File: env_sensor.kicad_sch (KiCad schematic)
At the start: 21 parts, among them J1 E Paper, J3 Barrel_Jack, J4 LED_OUTPUT, J5 Conn_01x02_Pin, J6 Conn_01x04_Socket, J6 ESP_Debugger, Q1 NMOS, Q2 NMOS, Q3 NMOS, U1 ESP32-DevKitC, U1 MH-Z19B, U5 BME280

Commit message: update MOS
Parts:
- Q1, Q2: footprint 2SK4017:TO230P230X650X740-3P -> env-sensor:SOT-23
- Q3: footprint 2SK4017:TO230P230X650X740-3P -> env-sensor:SOT-23; LCSC (none) -> C916396
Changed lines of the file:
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@@
 			)
 		)
-		(property "Footprint" "2SK4017:TO230P230X650X740-3P"
+		(property "Footprint" "env-sensor:SOT-23"
 			(at 58.42 64.77 0)
 			(effects
@@
 			)
 		)
-		(property "Footprint" "2SK4017:TO230P230X650X740-3P"
+		(property "Footprint" "env-sensor:SOT-23"
 			(at 58.42 39.37 0)
 			(effects
@@
 			)
 		)
-		(property "Footprint" "2SK4017:TO230P230X650X740-3P"
+		(property "Footprint" "env-sensor:SOT-23"
 			(at 58.42 90.17 0)
 			(effects
@@
 			)
 		)
-		(property "Sim.Pins" "1=D 2=G 3=S"
+		(property "Sim.Pins" "1=G 2=S 3=D"
 			(at 53.34 107.95 0)
 			(effects
 				(font
+					(size 1.27 1.27)
+				)
+				(hide yes)
+			)
+		)
+		(property "LCSC" "C916396"
+			(at 53.34 92.71 0)
+			(effects
+				(font

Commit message: add drv8847 (Working)
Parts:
- added R4, R5: 330m, Resistor_SMD:R_0603_1608Metric, symbol Device:R
- added U3: DRV8847SPWR, Package_SO:TSSOP-16_4.4x5mm_P0.65mm, symbol Driver_Motor:DRV8847SPWR
- Q1, Q2: LCSC (none) -> C916396
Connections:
- net GND: now also R4.2, R5.2, U3.13 (GND)
- net SCL: now also U3.11 (SCL)
- net SDA: now also U3.14 (SDA)
- new net: R4.1, U3.3 (ISEN12)
- new net: R5.1, U3.6 (ISEN34)

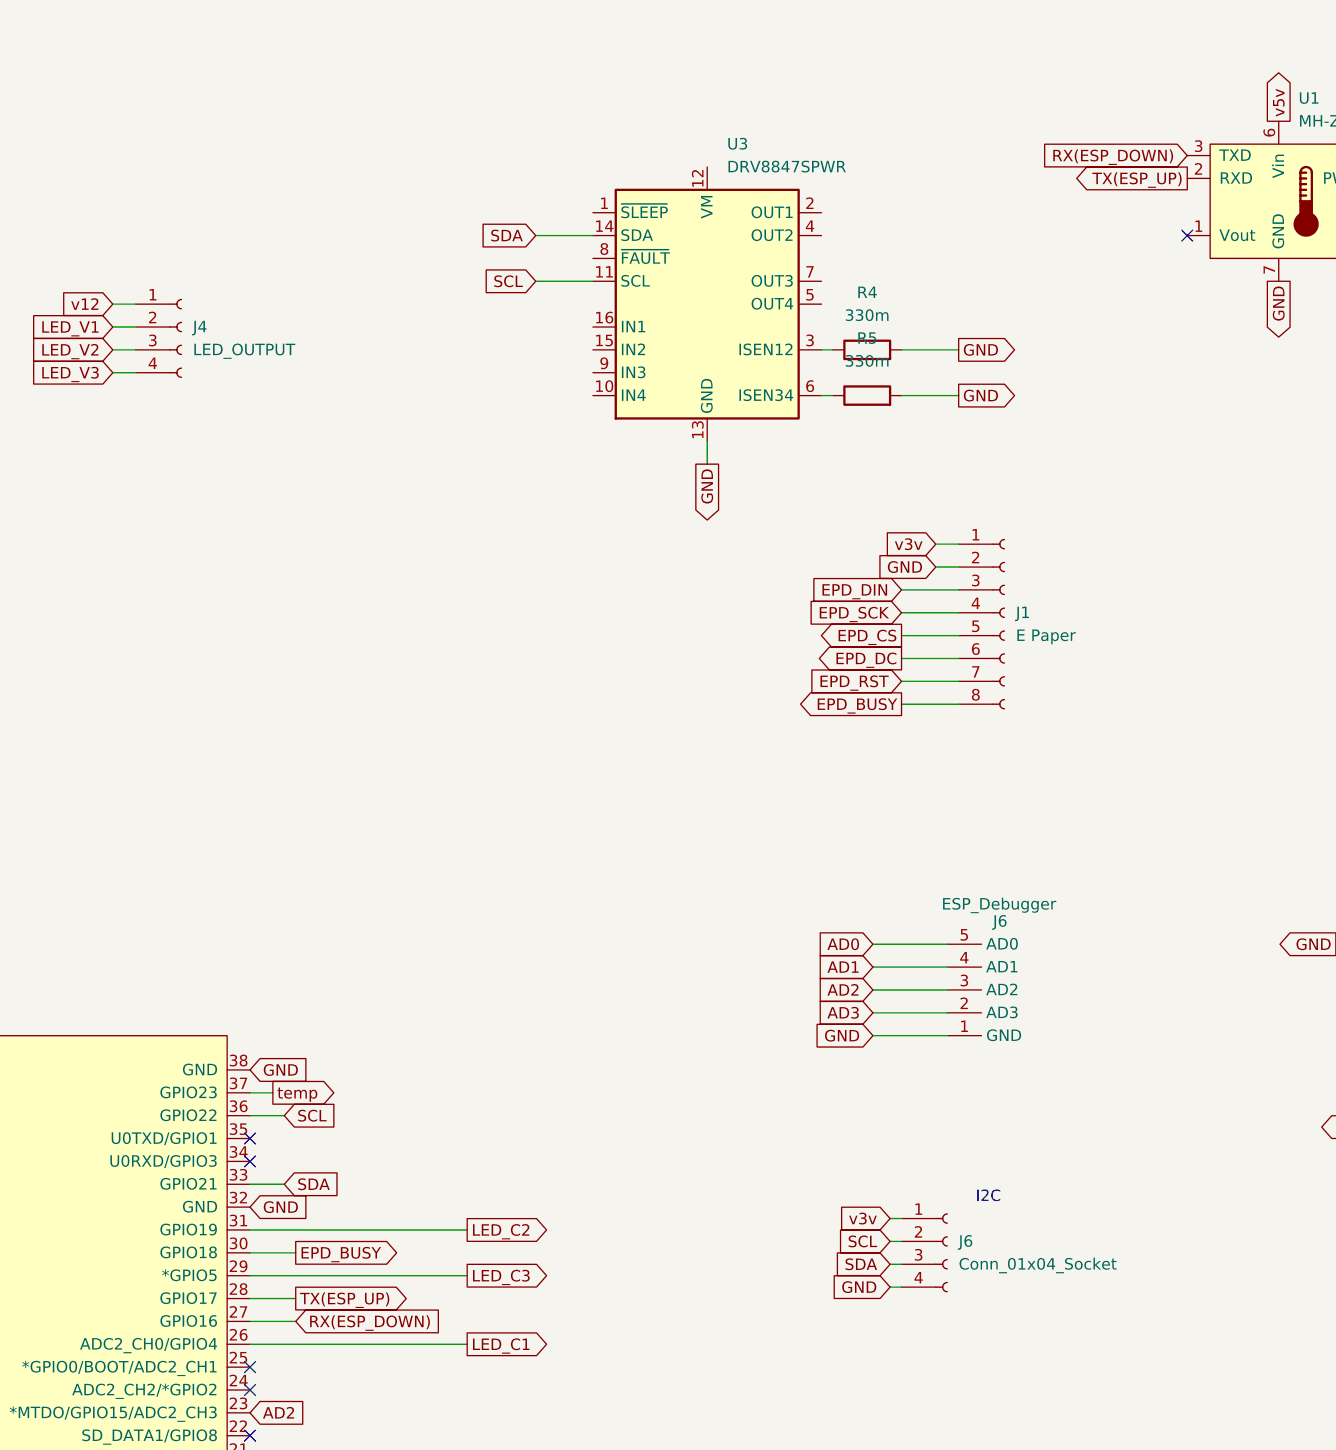
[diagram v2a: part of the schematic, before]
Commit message: add motor drivers
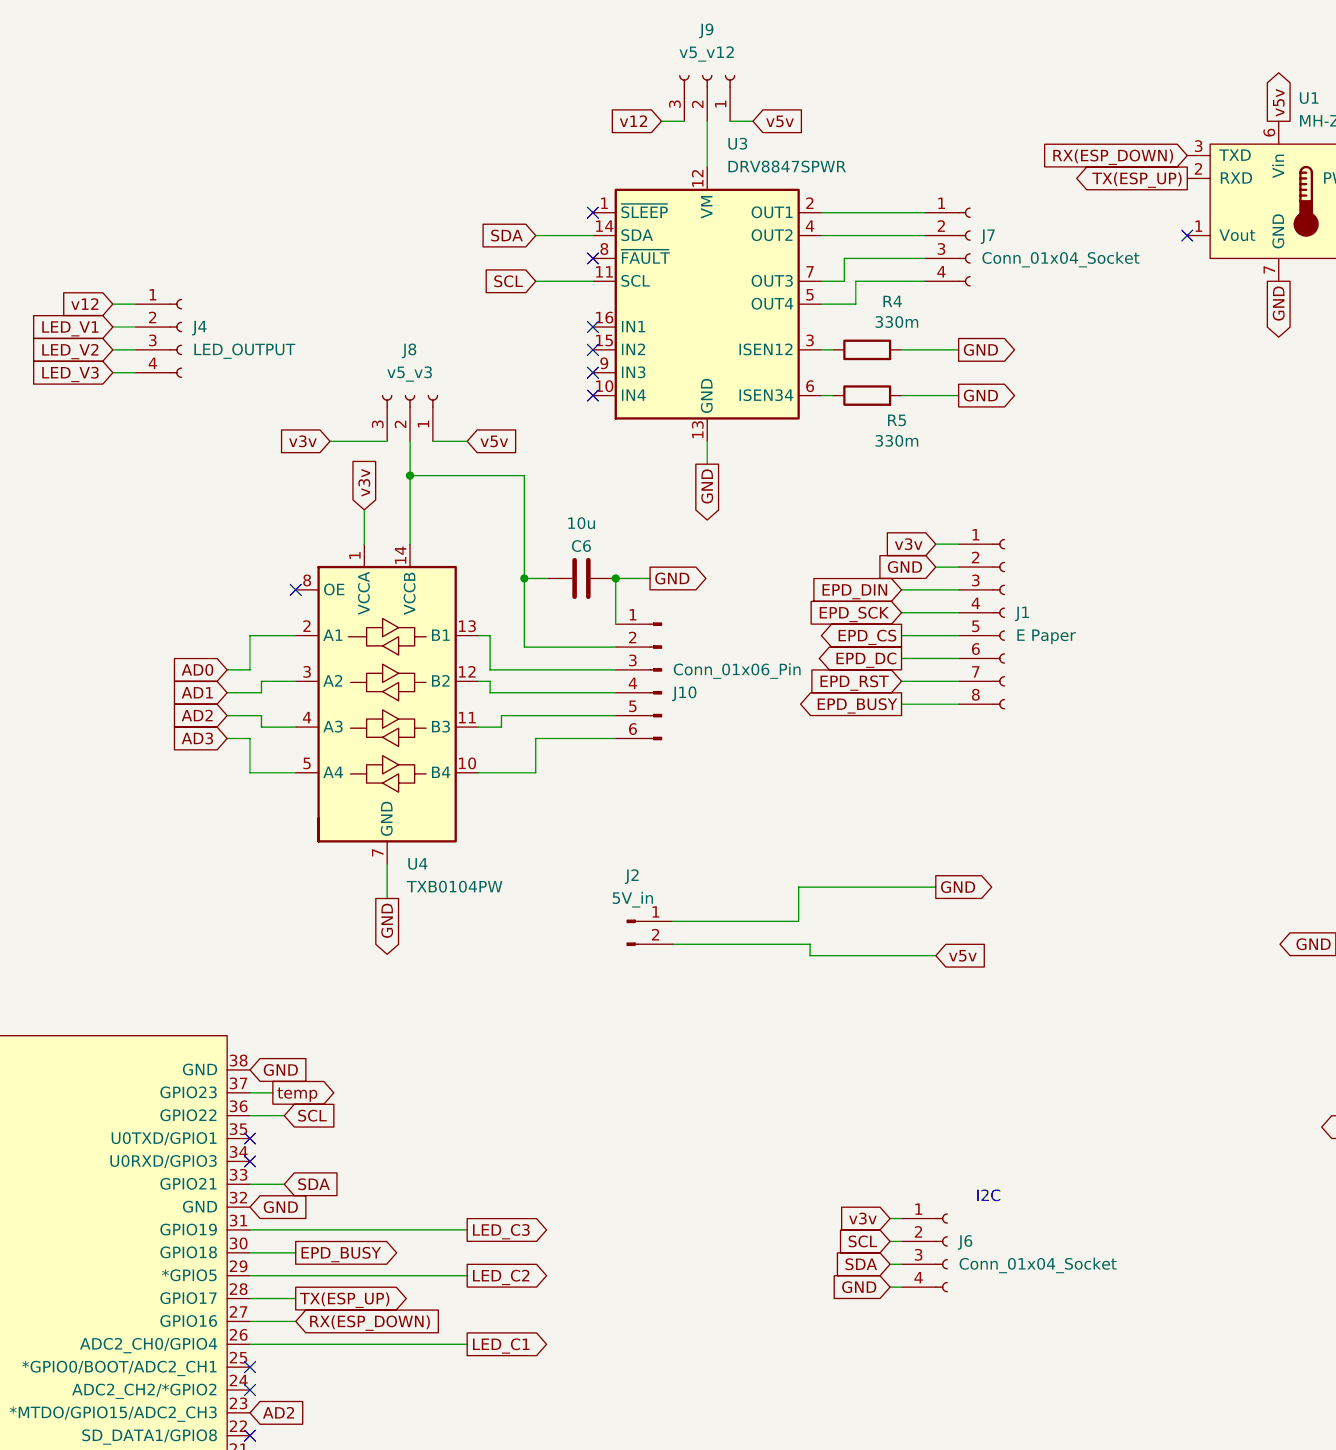
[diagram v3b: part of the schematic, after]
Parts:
- removed J6: ESP_Debugger, Connector_PinSocket_2.54mm:PinSocket_1x05_P2.54mm_Vertical, symbol PonchaLib:ESP_Debugger
- added C6: 10u, Capacitor_SMD:C_0603_1608Metric, symbol Device:C
- added J10: Conn_01x06_Pin, Connector_PinSocket_2.54mm:PinSocket_1x06_P2.54mm_Vertical, symbol Connector:Conn_01x06_Pin
- added J2: 5V_in, Connector_PinSocket_2.54mm:PinSocket_1x02_P2.54mm_Vertical, symbol Connector:Conn_01x02_Pin
- added J7: Conn_01x04_Socket, Connector_PinSocket_2.54mm:PinSocket_1x04_P2.54mm_Vertical, symbol Connector:Conn_01x04_Socket
- added J8: v5_v3, Connector_PinSocket_2.54mm:PinSocket_1x03_P2.54mm_Vertical, symbol Connector:Conn_01x03_Socket
- added J9: v5_v12, Connector_PinSocket_2.54mm:PinSocket_1x03_P2.54mm_Vertical, symbol Connector:Conn_01x03_Socket
- added U4: TXB0104PW, Package_SO:TSSOP-14_4.4x5mm_P0.65mm, symbol Logic_LevelTranslator:TXB0104PW
- J6: footprint (none) -> Connector_PinSocket_2.54mm:PinSocket_1x04_P2.54mm_Vertical
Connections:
- net AD0: now also U4.2 (A1)
- net AD1: now also U4.3 (A2)
- net AD2: now also U4.4 (A3)
- net AD3: now also U4.5 (A4)
- net GND: now also C6.1, J10.1 (Pin_1), J2.1 (Pin_1), U4.7 (GND)
- net LED_C2: now also U1.29 (*GPIO5); no longer U1.31 (GPIO19)
- net LED_C3: now also U1.31 (GPIO19); no longer U1.29 (*GPIO5)
- net v12: now also J9.3 (Pin_3)
- net v3v: now also J8.3 (Pin_3), U4.1 (VCCA)
- net v5v: now also J2.2 (Pin_2), J8.1 (Pin_1), J9.1 (Pin_1)
- net at U3.12 (VM): now also J9.2 (Pin_2)
- net at U3.2 (OUT1): now also J7.1 (Pin_1)
- net at U3.4 (OUT2): now also J7.2 (Pin_2)
- net at U3.5 (OUT4): now also J7.4 (Pin_4)
- net at U3.7 (OUT3): now also J7.3 (Pin_3)
- new net: C6.2, J10.2 (Pin_2), J8.2 (Pin_2), U4.14 (VCCB)
- new net: J10.3 (Pin_3), U4.13 (B1)
- new net: J10.4 (Pin_4), U4.12 (B2)
- new net: J10.5 (Pin_5), U4.11 (B3)
- new net: J10.6 (Pin_6), U4.10 (B4)
- no-connect marks 18 -> 25

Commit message: update pcb
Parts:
- C6: LCSC C141660 -> C267437
- R1, R2: LCSC C23164 -> C99782
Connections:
- net GND: now also C6.2; no longer C6.1
- net at J10.2 (Pin_2), J8.2 (Pin_2), U4.14 (VCCB): now also C6.1; no longer C6.2
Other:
- moved on the sheet: C1, C4, C5, C6, J1, J10, J2, J3, J4, J5, J6, J7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

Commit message: update bom
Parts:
- C6: LCSC C267437 -> C466783
- J1, J2, J3, J4, J5, J6, J7, J8, J9, U1: now left out of the parts list
- R1, R2: LCSC C99782 -> C23162
- R3: LCSC C863146 -> C22936
- R4, R5: LCSC (none) -> C22978
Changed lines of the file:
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@@
 			)
 		)
-		(property "LCSC" "C267437"
+		(property "LCSC" "C466783"
 			(at 114.3 83.82 90)
 			(effects
@@
 		(unit 1)
 		(exclude_from_sim no)
-		(in_bom yes)
-		(on_board yes)
+		(in_bom no)
+		(on_board no)
 		(dnp no)
 		(fields_autoplaced yes)
@@
 		(unit 1)
 		(exclude_from_sim no)
-		(in_bom yes)
-		(on_board yes)
+		(in_bom no)
+		(on_board no)
 		(dnp no)
 		(fields_autoplaced yes)
@@
 		(unit 1)
 		(exclude_from_sim no)
-		(in_bom yes)
-		(on_board yes)
+		(in_bom no)
+		(on_board no)
 		(dnp no)
 		(fields_autoplaced yes)
@@
 			)
 		)
+		(property "LCSC" "C22978"
+			(at 175.26 54.61 90)
+			(effects
+				(font
+					(size 1.27 1.27)
+				)
+				(hide yes)
+			)
+		)
 		(pin "1"
 		)
@@
 			)
 		)
-		(property "LCSC" "C99782"
+		(property "LCSC" "C23162"
 			(at 238.76 156.21 0)
 			(effects
@@
 			)
 		)
-		(property "LCSC" "C863146"
+		(property "LCSC" "C22936"
 			(at 242.57 27.94 0)
 			(effects
@@
 		(unit 1)
 		(exclude_from_sim no)
-		(in_bom yes)
-		(on_board yes)
+		(in_bom no)
+		(on_board no)
 		(dnp no)
 		(property "Reference" "J8"
@@
 		(unit 1)
 		(exclude_from_sim no)
-		(in_bom yes)
-		(on_board yes)
+		(in_bom no)
+		(on_board no)
 		(dnp no)
 		(property "Reference" "J9"
@@
 		(unit 1)
 		(exclude_from_sim no)
-		(in_bom yes)
-		(on_board yes)
+		(in_bom no)
+		(on_board no)
 		(dnp no)
 		(property "Reference" "U1"
@@
 			)
 		)
-		(property "LCSC" "C99782"
+		(property "LCSC" "C23162"
 			(at 234.95 146.05 0)
 			(effects
@@
 		(unit 1)
 		(exclude_from_sim no)
-		(in_bom yes)
-		(on_board yes)
+		(in_bom no)
+		(on_board no)
 		(dnp no)
 		(fields_autoplaced yes)
@@
 		(unit 1)
 		(exclude_from_sim no)
-		(in_bom yes)
-		(on_board yes)
+		(in_bom no)
+		(on_board no)
 		(dnp no)
 		(fields_autoplaced yes)
@@
 			)
 		)
+		(property "LCSC" "C22978"
+			(at 175.26 59.69 90)
+			(effects
+				(font
+					(size 1.27 1.27)
+				)
+				(hide yes)
+			)
+		)
 		(pin "1"
 		)
@@
 		(unit 1)
 		(exclude_from_sim no)
-		(in_bom yes)
-		(on_board yes)
+		(in_bom no)
+		(on_board no)
 		(dnp no)
 		(fields_autoplaced yes)
@@
 		(unit 1)
 		(exclude_from_sim no)
-		(in_bom yes)
-		(on_board yes)
+		(in_bom no)
+		(on_board no)
 		(dnp no)
 		(fields_autoplaced yes)
@@
 		(unit 1)
 		(exclude_from_sim no)
-		(in_bom yes)
-		(on_board yes)
+		(in_bom no)
+		(on_board no)
 		(dnp no)
 		(fields_autoplaced yes)

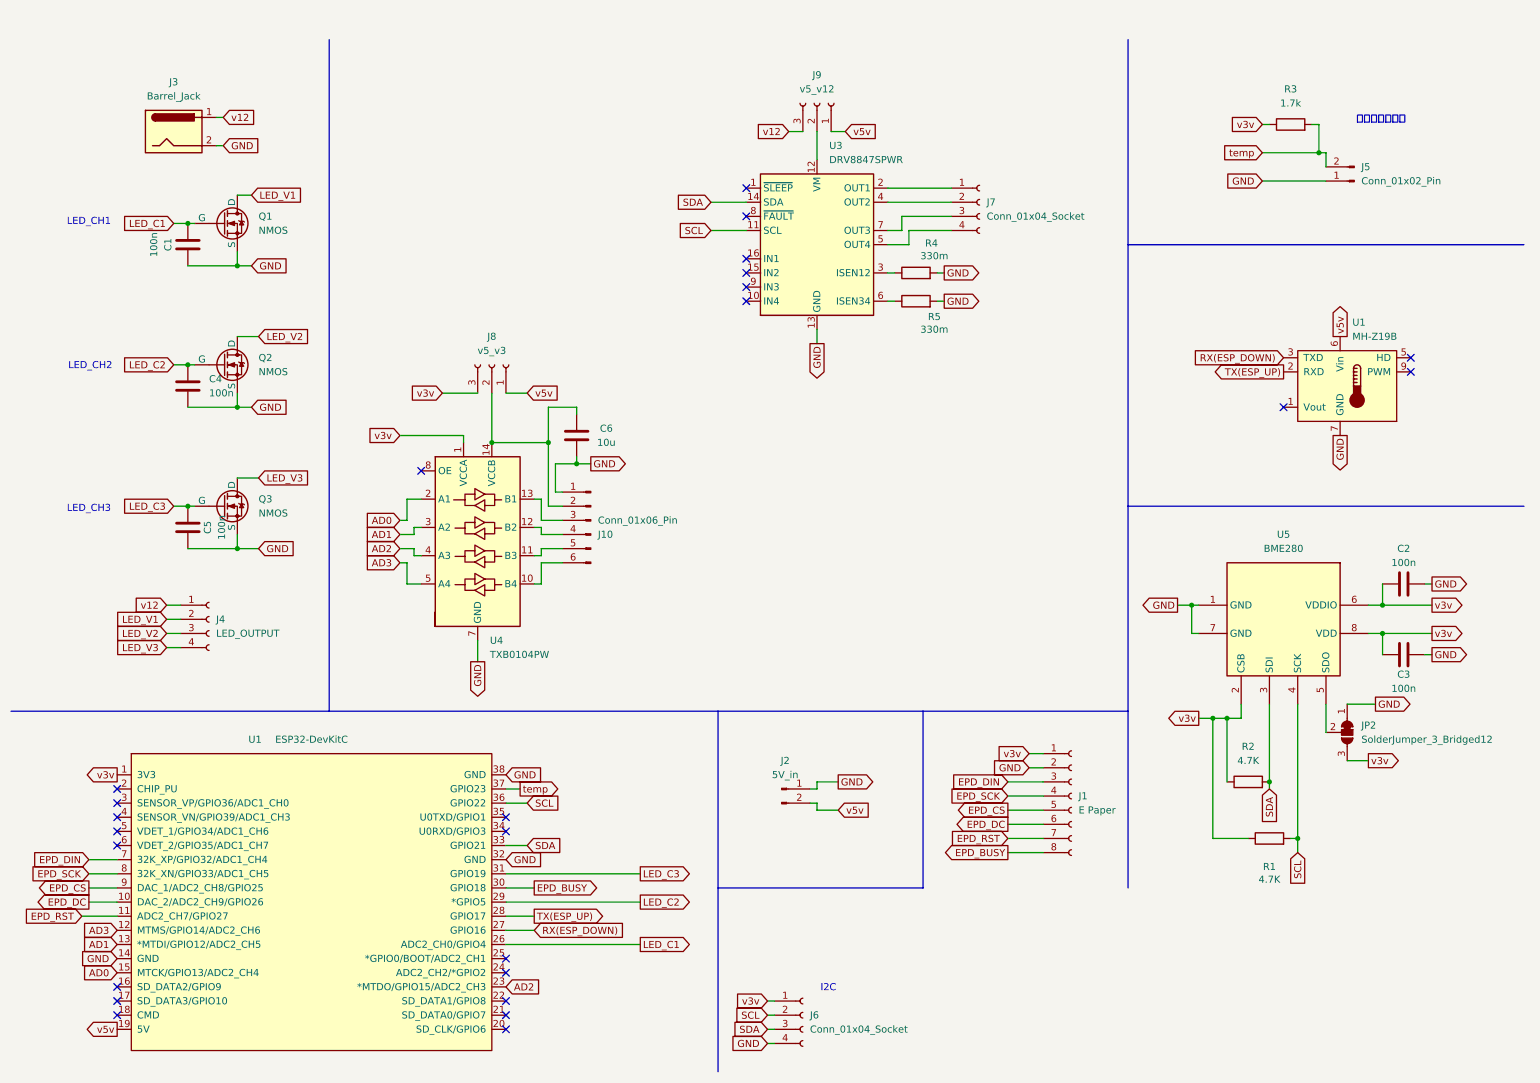
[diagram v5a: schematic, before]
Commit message: delete motor driver
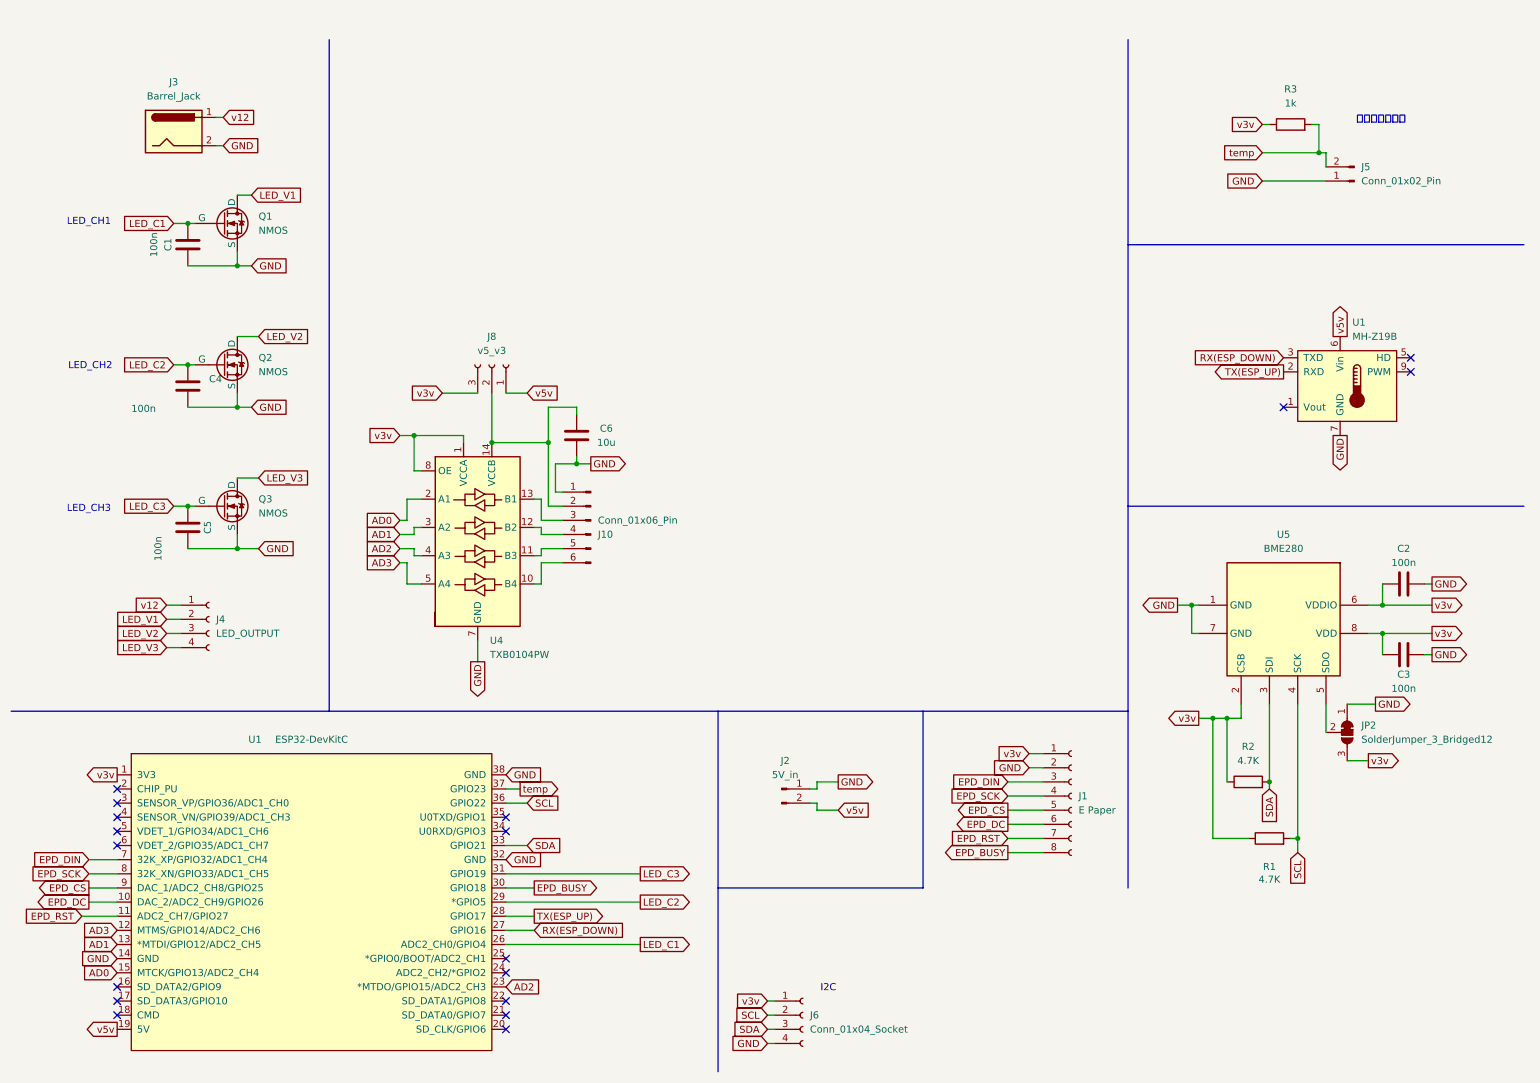
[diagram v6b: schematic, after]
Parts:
- removed J7: Conn_01x04_Socket, Connector_PinSocket_2.54mm:PinSocket_1x04_P2.54mm_Vertical, symbol Connector:Conn_01x04_Socket
- removed J9: v5_v12, Connector_PinSocket_2.54mm:PinSocket_1x03_P2.54mm_Vertical, symbol Connector:Conn_01x03_Socket
- removed R4, R5: 330m, Resistor_SMD:R_0603_1608Metric, symbol Device:R
- removed U3: DRV8847SPWR, Package_SO:TSSOP-16_4.4x5mm_P0.65mm, symbol Driver_Motor:DRV8847SPWR
- C6: LCSC C466783 -> C5137578
- R3: value 1.7k -> 1k; LCSC C22936 -> C21190
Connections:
- net v3v: now also U4.8 (OE)
- no-connect marks 25 -> 18
